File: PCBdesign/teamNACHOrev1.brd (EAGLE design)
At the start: 100 x 80 mm, 17 parts, among them Q2 TK40E06N1

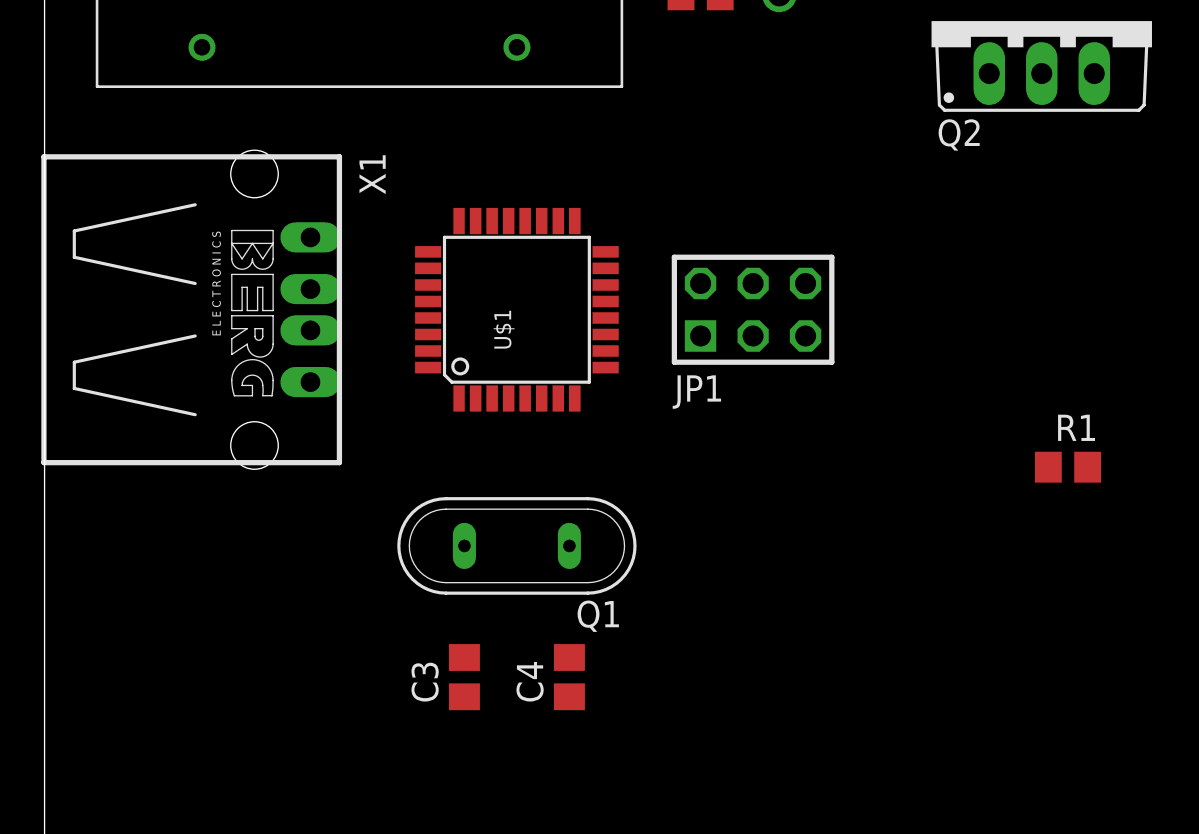
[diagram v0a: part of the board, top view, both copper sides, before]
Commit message: Fixed USB
Flipped which pins on USB are ground and power. Also may have to make
own lib for LM317, they don’t have the correct pcb package we need.
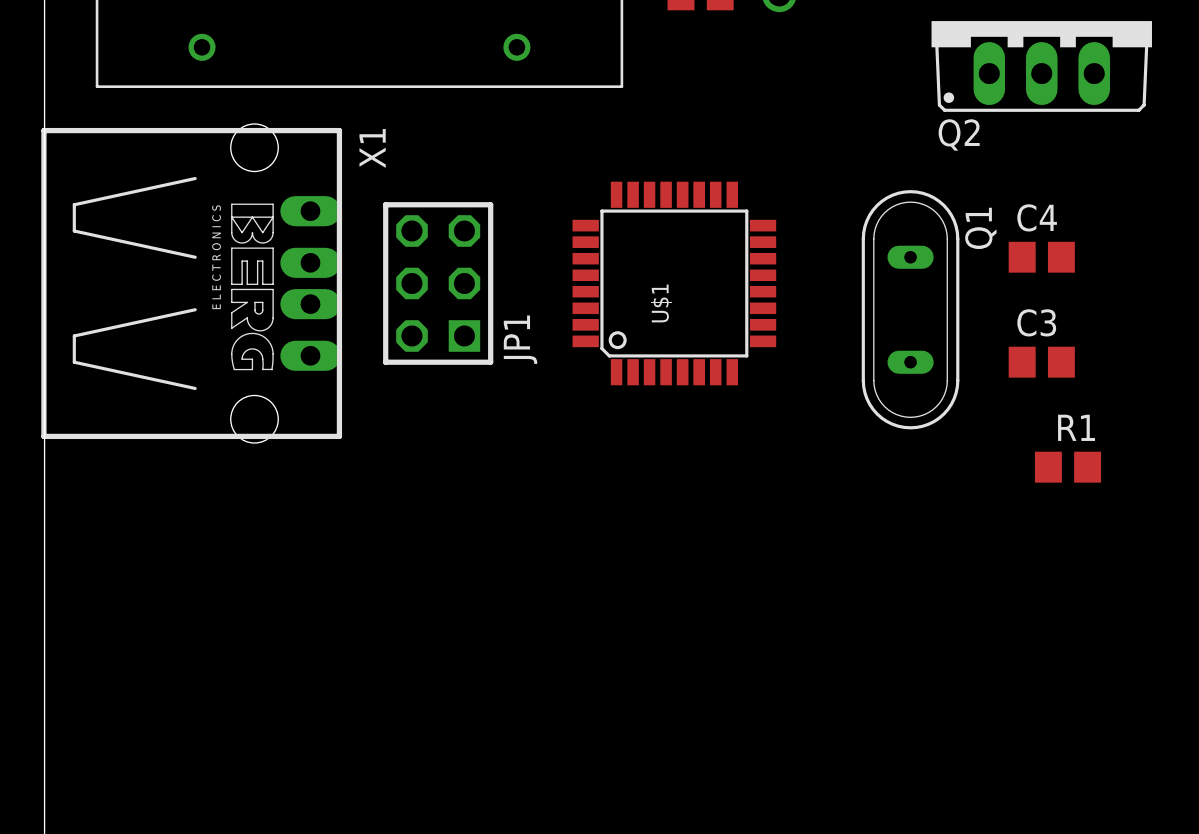
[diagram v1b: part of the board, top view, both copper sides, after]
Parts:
- moved C3 31.8 mm to (48.3, 38.1), turned to 0 degrees
- moved C4 30.6 mm to (48.3, 43.2), turned to 0 degrees
- moved Q1 22.2 mm to (41.9, 40.6), turned to 270 degrees
- moved JP1 15.3 mm to (19.1, 41.9), turned to 90 degrees
- moved U$1 7.73 mm to (30.5, 41.9)
- moved X1 1.27 mm to (10.2, 41.9)
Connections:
- net +5V: now also X1.4; no longer X1.1
- net GND: now also X1.1; no longer X1.4
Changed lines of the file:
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@@
 <element name="C1" library="rcl" package="C0805" value="10u" x="44.45" y="64.77"/>
 <element name="C2" library="rcl" package="C0805" value="0.1u" x="40.64" y="67.31"/>
-<element name="C3" library="rcl" package="C0805" value="22u" x="20.32" y="22.86" rot="R90"/>
-<element name="C4" library="rcl" package="C0805" value="22u" x="25.4" y="22.86" rot="R90"/>
+<element name="C3" library="rcl" package="C0805" value="22u" x="48.26" y="38.1"/>
+<element name="C4" library="rcl" package="C0805" value="22u" x="48.26" y="43.18"/>
 <element name="C5" library="rcl" package="C0805" value="10u" x="53.34" y="66.04"/>
 <element name="C6" library="rcl" package="C0805" value="10u" x="46.99" y="73.66" rot="R270"/>
 <element name="D1" library="diode" package="DO41-10" value="1N4004" x="35.56" y="60.96" rot="R90"/>
 <element name="D2" library="diode" package="DO41-10" value="1N4004" x="36.83" y="74.93" rot="R180"/>
-<element name="JP1" library="avr-7" package="AVR-ISP-6" value="AVR-ISP-6VERT" x="34.29" y="40.64"/>
-<element name="Q1" library="special" package="QS" value="" x="22.86" y="29.21" rot="R180"/>
+<element name="JP1" library="avr-7" package="AVR-ISP-6" value="AVR-ISP-6VERT" x="19.05" y="41.91" rot="R90"/>
+<element name="Q1" library="special" package="QS" value="" x="41.91" y="40.64" rot="R270"/>
 <element name="Q2" library="transistor-power" package="TO220BV" value="TK40E06N1" x="48.26" y="54.61"/>
 <element name="R1" library="rcl" package="R0805" value="4.7K" x="49.53" y="33.02"/>
 <element name="R2" library="resistor" package="R0805" value="1K" x="31.75" y="55.88"/>
 <element name="R3" library="rcl" package="M0805" value="12" x="62.23" y="74.93"/>
-<element name="U$1" library="ATMEGA328p" package="TQFP32" value="ATMEGA328P" x="22.86" y="40.64" rot="R90"/>
+<element name="U$1" library="ATMEGA328p" package="TQFP32" value="ATMEGA328P" x="30.48" y="41.91" rot="R90"/>
 <element name="U$2" library="PE-63388NL" package="PE-633XXNL" value="PE-63388NL" x="7.62" y="71.12"/>
-<element name="X1" library="con-berg" package="PN87520" value="" x="10.16" y="40.64" rot="R270">
-<attribute name="OC_NEWARK" value="unknown" x="10.16" y="40.64" size="1.778" layer="27" rot="R270" display="off"/>
-<attribute name="MF" value="" x="10.16" y="40.64" size="1.778" layer="27" rot="R270" display="off"/>
-<attribute name="MPN" value="" x="10.16" y="40.64" size="1.778" layer="27" rot="R270" display="off"/>
-<attribute name="OC_FARNELL" value="unknown" x="10.16" y="40.64" size="1.778" layer="27" rot="R270" display="off"/>
+<element name="X1" library="con-berg" package="PN87520" value="" x="10.16" y="41.91" rot="R270">
+<attribute name="OC_NEWARK" value="unknown" x="10.16" y="41.91" size="1.778" layer="27" rot="R270" display="off"/>
+<attribute name="MF" value="" x="10.16" y="41.91" size="1.778" layer="27" rot="R270" display="off"/>
+<attribute name="MPN" value="" x="10.16" y="41.91" size="1.778" layer="27" rot="R270" display="off"/>
+<attribute name="OC_FARNELL" value="unknown" x="10.16" y="41.91" size="1.778" layer="27" rot="R270" display="off"/>
 </element>
 </elements>
@@
 <contactref element="U$1" pad="21"/>
 <contactref element="JP1" pad="6"/>
-<contactref element="X1" pad="4"/>
 <contactref element="Q2" pad="S"/>
-<wire x1="45.4" y1="64.77" x2="41.59" y2="67.31" width="0" layer="19" extent="1-1"/>
-<wire x1="20.32" y1="23.81" x2="45.4" y2="64.77" width="0" layer="19" extent="1-1"/>
-<wire x1="25.4" y1="23.81" x2="20.32" y2="23.81" width="0" layer="19" extent="1-1"/>
-<wire x1="36.83" y1="41.91" x2="25.4" y2="23.81" width="0" layer="19" extent="1-1"/>
-<wire x1="21.66" y1="36.3474" x2="36.83" y2="41.91" width="0" layer="19" extent="1-1"/>
-<wire x1="23.26" y1="36.3474" x2="21.66" y2="36.3474" width="0" layer="19" extent="1-1"/>
-<wire x1="22.46" y1="44.9326" x2="21.66" y2="36.3474" width="0" layer="19" extent="1-1"/>
-<wire x1="50.8" y1="52.07" x2="36.83" y2="41.91" width="0" layer="19" extent="1-1"/>
-<wire x1="12.87" y1="37.14" x2="50.8" y2="52.07" width="0" layer="19" extent="1-1"/>
+<contactref element="X1" pad="1"/>
+<wire x1="41.59" y1="67.31" x2="45.4" y2="64.77" width="0" layer="19" extent="1-1"/>
+<wire x1="50.8" y1="52.07" x2="45.4" y2="64.77" width="0" layer="19" extent="1-1"/>
+<wire x1="17.78" y1="44.45" x2="50.8" y2="52.07" width="0" layer="19" extent="1-1"/>
+<wire x1="30.88" y1="37.6174" x2="17.78" y2="44.45" width="0" layer="19" extent="1-1"/>
+<wire x1="29.28" y1="37.6174" x2="30.88" y2="37.6174" width="0" layer="19" extent="1-1"/>
+<wire x1="30.08" y1="46.2026" x2="30.88" y2="37.6174" width="0" layer="19" extent="1-1"/>
+<wire x1="49.21" y1="38.1" x2="29.28" y2="37.6174" width="0" layer="19" extent="1-1"/>
+<wire x1="49.21" y1="43.18" x2="49.21" y2="38.1" width="0" layer="19" extent="1-1"/>
+<wire x1="12.87" y1="45.41" x2="49.21" y2="38.1" width="0" layer="19" extent="1-1"/>
 </signal>
 <signal name="N$2">
@@
 <contactref element="Q1" pad="2"/>
 <contactref element="C3" pad="1"/>
-<wire x1="24.86" y1="36.3474" x2="20.32" y2="29.21" width="0" layer="19" extent="1-1"/>
-<wire x1="20.32" y1="21.91" x2="20.32" y2="29.21" width="0" layer="19" extent="1-1"/>
+<wire x1="32.48" y1="37.6174" x2="41.91" y2="38.1" width="0" layer="19" extent="1-1"/>
+<wire x1="47.31" y1="38.1" x2="41.91" y2="38.1" width="0" layer="19" extent="1-1"/>
 </signal>
 <signal name="N$3">
@@
 <contactref element="Q1" pad="1"/>
 <contactref element="C4" pad="1"/>
-<wire x1="25.66" y1="36.3474" x2="25.4" y2="29.21" width="0" layer="19" extent="1-1"/>
-<wire x1="25.4" y1="21.91" x2="25.4" y2="29.21" width="0" layer="19" extent="1-1"/>
+<wire x1="33.28" y1="37.6174" x2="41.91" y2="43.18" width="0" layer="19" extent="1-1"/>
+<wire x1="47.31" y1="43.18" x2="41.91" y2="43.18" width="0" layer="19" extent="1-1"/>
 </signal>
 <signal name="+5V">
@@
 <contactref element="R2" pad="2"/>
 <contactref element="U$2" pad="P1"/>
-<contactref element="X1" pad="1"/>
-<wire x1="7.62" y1="71.12" x2="12.87" y2="44.14" width="0" layer="19" extent="1-1"/>
-<wire x1="31.75" y1="41.91" x2="7.62" y2="71.12" width="0" layer="19" extent="1-1"/>
-<wire x1="22.46" y1="36.3474" x2="31.75" y2="41.91" width="0" layer="19" extent="1-1"/>
-<wire x1="24.06" y1="36.3474" x2="22.46" y2="36.3474" width="0" layer="19" extent="1-1"/>
-<wire x1="23.26" y1="44.9326" x2="22.46" y2="36.3474" width="0" layer="19" extent="1-1"/>
-<wire x1="24.86" y1="44.9326" x2="23.26" y2="44.9326" width="0" layer="19" extent="1-1"/>
-<wire x1="52.39" y1="66.04" x2="31.75" y2="41.91" width="0" layer="19" extent="1-1"/>
-<wire x1="32.7" y1="55.88" x2="52.39" y2="66.04" width="0" layer="19" extent="1-1"/>
-<wire x1="50.48" y1="33.02" x2="32.7" y2="55.88" width="0" layer="19" extent="1-1"/>
+<contactref element="X1" pad="4"/>
 <wire x1="43.5" y1="64.77" x2="52.39" y2="66.04" width="0" layer="19" extent="1-1"/>
 <wire x1="39.69" y1="67.31" x2="43.5" y2="64.77" width="0" layer="19" extent="1-1"/>
+<wire x1="32.7" y1="55.88" x2="39.69" y2="67.31" width="0" layer="19" extent="1-1"/>
+<wire x1="32.48" y1="46.2026" x2="32.7" y2="55.88" width="0" layer="19" extent="1-1"/>
+<wire x1="30.88" y1="46.2026" x2="32.48" y2="46.2026" width="0" layer="19" extent="1-1"/>
+<wire x1="17.78" y1="39.37" x2="32.48" y2="46.2026" width="0" layer="19" extent="1-1"/>
+<wire x1="31.68" y1="37.6174" x2="32.48" y2="46.2026" width="0" layer="19" extent="1-1"/>
+<wire x1="30.08" y1="37.6174" x2="31.68" y2="37.6174" width="0" layer="19" extent="1-1"/>
+<wire x1="50.48" y1="33.02" x2="17.78" y2="39.37" width="0" layer="19" extent="1-1"/>
+<wire x1="7.62" y1="71.12" x2="32.7" y2="55.88" width="0" layer="19" extent="1-1"/>
+<wire x1="12.87" y1="38.41" x2="30.08" y2="37.6174" width="0" layer="19" extent="1-1"/>
 </signal>
 <signal name="SCK">
 <contactref element="JP1" pad="3"/>
 <contactref element="U$1" pad="17"/>
-<wire x1="34.29" y1="39.37" x2="25.66" y2="44.9326" width="0" layer="19" extent="1-1"/>
+<wire x1="20.32" y1="41.91" x2="33.28" y2="46.2026" width="0" layer="19" extent="1-1"/>
 </signal>
 <signal name="RESET">
@@
 <contactref element="U$1" pad="29"/>
 <contactref element="R1" pad="1"/>
-<wire x1="36.83" y1="39.37" x2="18.5674" y2="40.24" width="0" layer="19" extent="1-1"/>
-<wire x1="48.58" y1="33.02" x2="36.83" y2="39.37" width="0" layer="19" extent="1-1"/>
+<wire x1="20.32" y1="44.45" x2="26.1874" y2="41.51" width="0" layer="19" extent="1-1"/>
+<wire x1="48.58" y1="33.02" x2="20.32" y2="44.45" width="0" layer="19" extent="1-1"/>
 </signal>
 <signal name="MISO">
 <contactref element="U$1" pad="16"/>
 <contactref element="JP1" pad="1"/>
-<wire x1="31.75" y1="39.37" x2="27.1526" y2="43.44" width="0" layer="19" extent="1-1"/>
+<wire x1="20.32" y1="39.37" x2="34.7726" y2="44.71" width="0" layer="19" extent="1-1"/>
 </signal>
 <signal name="MOSI">
 <contactref element="U$1" pad="15"/>
 <contactref element="JP1" pad="4"/>
-<wire x1="34.29" y1="41.91" x2="27.1526" y2="42.64" width="0" layer="19" extent="1-1"/>
+<wire x1="17.78" y1="41.91" x2="34.7726" y2="43.91" width="0" layer="19" extent="1-1"/>
 </signal>
 <signal name="N$4">
